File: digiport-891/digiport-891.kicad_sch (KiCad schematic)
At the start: 45 parts, among them J1 USB_C_Receptacle_USB2.0_16P, J2 PJ-320A, J3 PJ-320A, Q1 MMBT5551L, Q2 MMBT5551L, U1 USB2412-DZK-TR, U2 CM108B, Y1 24MHz

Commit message: add PNG of pcb and PDF of shcematic
1. PNG of PCB and PDF of schematic are added
2. Library path is changed to relative path.
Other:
- company: (none) -> BD5HLI
- title: (none) -> DigiPort-891
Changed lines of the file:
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@@
 	(generator_version "8.0")
 	(paper "A3")
+	(title_block
+		(title "DigiPort-891")
+		(company "BD5HLI")
+	)
 	(junction
 		(at 281.94 115.57)

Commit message: cable pinout file added
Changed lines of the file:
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@@
 (kicad_sch
-	(version 20231120)
+	(version 20250114)
 	(generator "eeschema")
-	(generator_version "8.0")
+	(generator_version "9.0")
 	(paper "A3")
 	(title_block
@@
 		(company "BD5HLI")
 	)
+	(text "USB Hub"
+		(exclude_from_sim no)
+		(at 28.194 24.384 0)
+		(effects
+			(font
+				(size 1.27 1.27)
+			)
+			(justify left bottom)
+		)
+	)
+	(text "Audio Codec, PTT switch"
+		(exclude_from_sim no)
+		(at 177.8 24.13 0)
+		(effects
+			(font
+				(size 1.27 1.27)
+			)
+			(justify left bottom)
+		)
+	)
+	(text "CM108 Config:\n- Playback & Recording (MODE low)\n- With Mixer / AA-Path Enable (MSEL high)\n- Line out Vpp = 2.5 Volts (VSEL low)\n- Bus Power with 100mA (PWRSEL high)\n- Use internal ADC (ADSEL low)\n- Normal Operation (TEST low)"
+		(exclude_from_sim no)
+		(at 177.8 146.05 0)
+		(effects
+			(font
+				(size 1.27 1.27)
+			)
+			(justify left bottom)
+		)
+	)
+	(text "USB1412 Config:\n- both ports are non-removable\n  (NON_REM1, SUSP_IND/NON_REM2 high at reset)\n- no high speed LED\n  (HS_IND low)"
+		(exclude_from_sim no)
+		(at 33.274 160.02 0)
+		(effects
+			(font
+				(size 1.27 1.27)
+			)
+			(justify left bottom)
+		)
+	)
 	(junction
 		(at 281.94 115.57)
@@
 		)
 	)
-	(text "USB Hub"
-		(exclude_from_sim no)
-		(at 28.194 24.384 0)
-		(effects
-			(font
-				(size 1.27 1.27)
-			)
-			(justify left bottom)
-		)
-	)
-	(text "Audio Codec, PTT switch"
-		(exclude_from_sim no)
-		(at 177.8 24.13 0)
-		(effects
-			(font
-				(size 1.27 1.27)
-			)
-			(justify left bottom)
-		)
-	)
-	(text "CM108 Config:\n- Playback & Recording (MODE low)\n- With Mixer / AA-Path Enable (MSEL high)\n- Line out Vpp = 2.5 Volts (VSEL low)\n- Bus Power with 100mA (PWRSEL high)\n- Use internal ADC (ADSEL low)\n- Normal Operation (TEST low)"
-		(exclude_from_sim no)
-		(at 177.8 146.05 0)
-		(effects
-			(font
-				(size 1.27 1.27)
-			)
-			(justify left bottom)
-		)
-	)
-	(text "USB1412 Config:\n- both ports are non-removable\n  (NON_REM1, SUSP_IND/NON_REM2 high at reset)\n- no high speed LED\n  (HS_IND low)"
-		(exclude_from_sim no)
-		(at 33.274 160.02 0)
-		(effects
-			(font
-				(size 1.27 1.27)
-			)
-			(justify left bottom)
-		)
-	)
 	(label "USBUP_D+"
 		(at 96.52 53.34 180)
-		(fields_autoplaced yes)
 		(effects
 			(font
@@
 	(label "USBDN2_D+"
 		(at 127 67.31 0)
-		(fields_autoplaced yes)
 		(effects
 			(font
@@
 	(label "RIG_AFIN"
 		(at 334.01 55.88 0)
-		(fields_autoplaced yes)
 		(effects
 			(font
@@
 	(label "USBDN1_D+"
 		(at 127 53.34 0)
-		(fields_autoplaced yes)
 		(effects
 			(font
@@
 	(label "USBDN1_D-"
 		(at 127 50.8 0)
-		(fields_autoplaced yes)
 		(effects
 			(font
@@
 	(label "USBUP_D-"
 		(at 96.52 55.88 180)
-		(fields_autoplaced yes)
 		(effects
 			(font
@@
 	(label "RIG_AFOUT"
 		(at 334.01 53.34 0)
-		(fields_autoplaced yes)
 		(effects
 			(font
@@
 	(label "USBDN2_D-"
 		(at 127 64.77 0)
-		(fields_autoplaced yes)
 		(effects
 			(font
@@
 		(at 320.04 50.8 0)
 		(unit 1)
-		(exclude_from_sim yes)
+		(exclude_from_sim no)
 		(in_bom no)
 		(on_board yes)
@@
 		(at 345.44 109.22 270)
 		(unit 1)
-		(exclude_from_sim yes)
+		(exclude_from_sim no)
 		(in_bom no)
 		(on_board yes)
@@
 		)
 	)
+	(embedded_fonts no)
 )

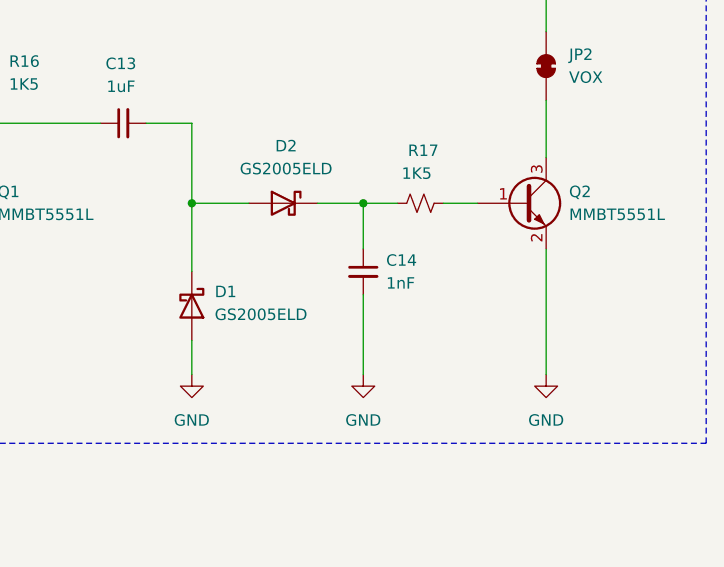
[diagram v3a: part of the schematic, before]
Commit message: C12 value corrected.
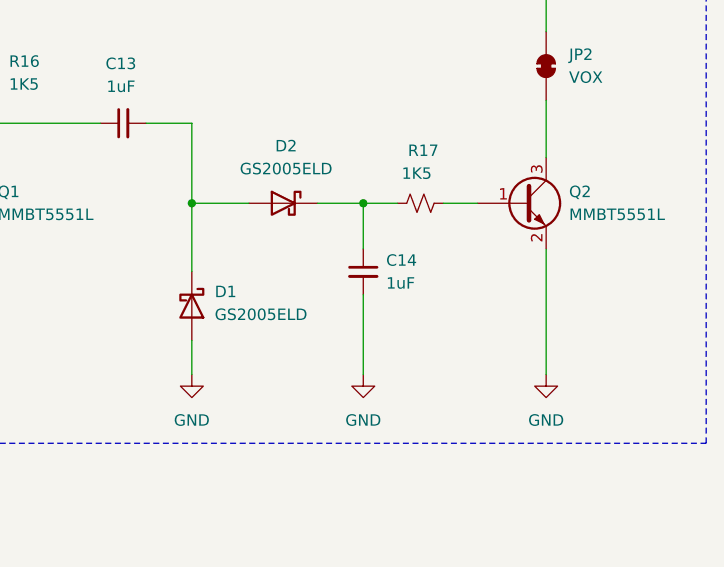
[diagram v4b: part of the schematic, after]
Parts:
- C14: value 1nF -> 1uF
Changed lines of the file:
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@@
 			)
 		)
-		(property "Value" "1nF"
+		(property "Value" "1uF"
 			(at 327.66 133.3562 0)
 			(effects
